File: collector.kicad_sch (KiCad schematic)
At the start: 2 parts, among them U14 CD74HCT32E

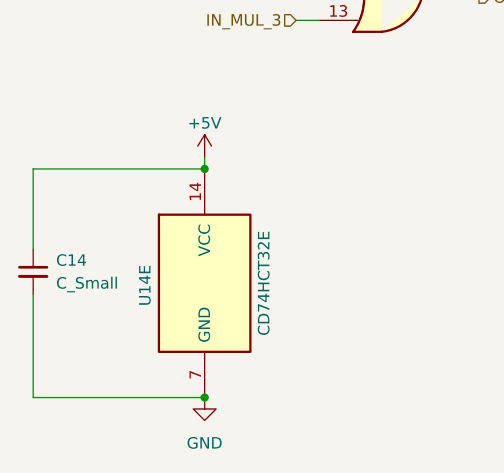
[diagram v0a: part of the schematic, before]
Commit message: chore: changed R and C ref to passive value
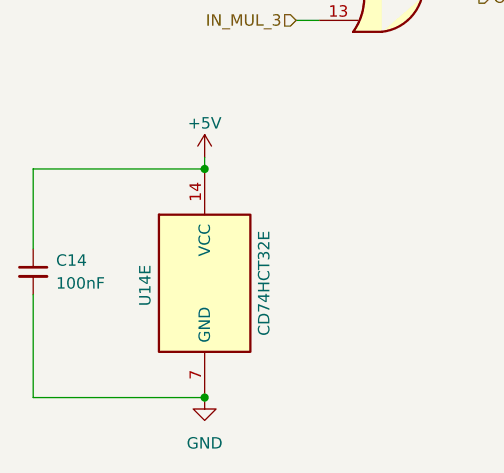
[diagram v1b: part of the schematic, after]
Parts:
- C14: value C_Small -> 100nF
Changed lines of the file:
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@@
 			)
 		)
-		(property "Value" "C_Small"
+		(property "Value" "100nF"
 			(at 54.61 127.0062 0)
 			(effects
